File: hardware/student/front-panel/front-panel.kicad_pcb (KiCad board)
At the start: 4 copper layers, 180 x 100 mm, 78 parts, among them J1 Panel link 2x20 female, J10 SMA, J11 SMA, J12 SMA, J13 SMA, J14 SMA, J15 SMA, J16 SMA, J17 SMA, J18 SMA, J19 SMA, J2 Panel link 2x20 female, J20 SMA, J21 SMA, J22 SMA, J23 SMA, J24 SMA, J25 SMA, J26 SMA, J3 Panel link 2x20 female, J30 OLED 0.96in module on 1x4 soc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, J31 KF128-2.54-10P, J32 KF128-5.0-2P, J33 Qwiic (vertical), J40 Module header 2x6 (shrouded), J411 KF301-5.0-2P, J412 KF301-5.0-2P, Q411 MMBT5551, Q412 MMBT5551, Q421 MMBT5551, Q422 MMBT5551, U401 6N137S-TA1-L, U402 6N137S-TA1-L, U410 SN74AHCT541PWR

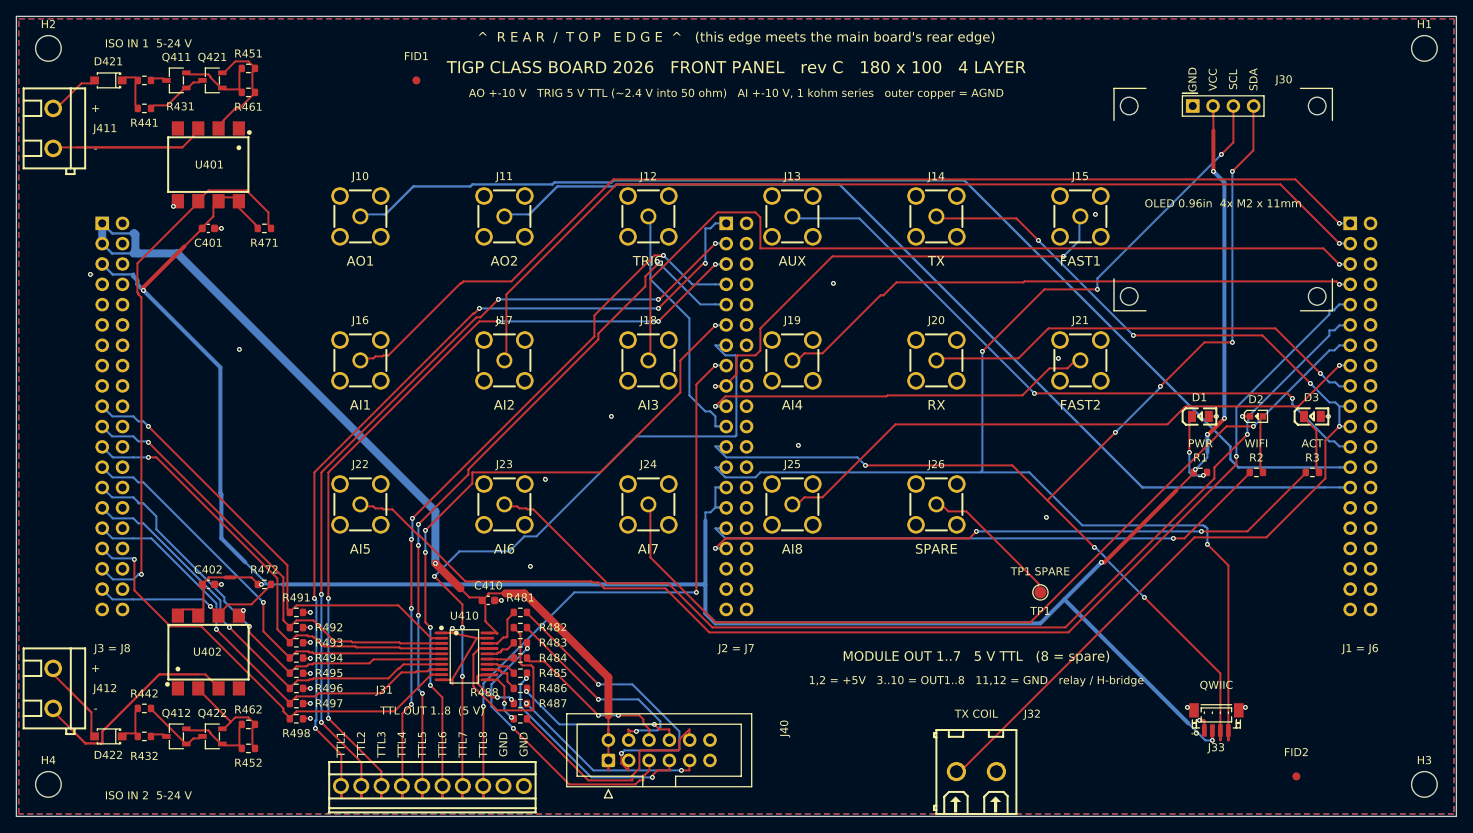
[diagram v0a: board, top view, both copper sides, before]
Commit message: v0.7d: relays and mains removed, MODULE OUT 1-7 (5 V TTL) on a shrouded 2x6 header on the front panel, isolated inputs moved to the panel, section C = the front-panel board (4-layer, 18 mm SMA grid, OLED clear of headers, unrouted student copy), main board re-placed; workbook, tutor guide, firmware docs, hardware docs updated (Decision #58)
Co-Authored-By: Claude Fable 5.1 <noreply@anthropic.com>
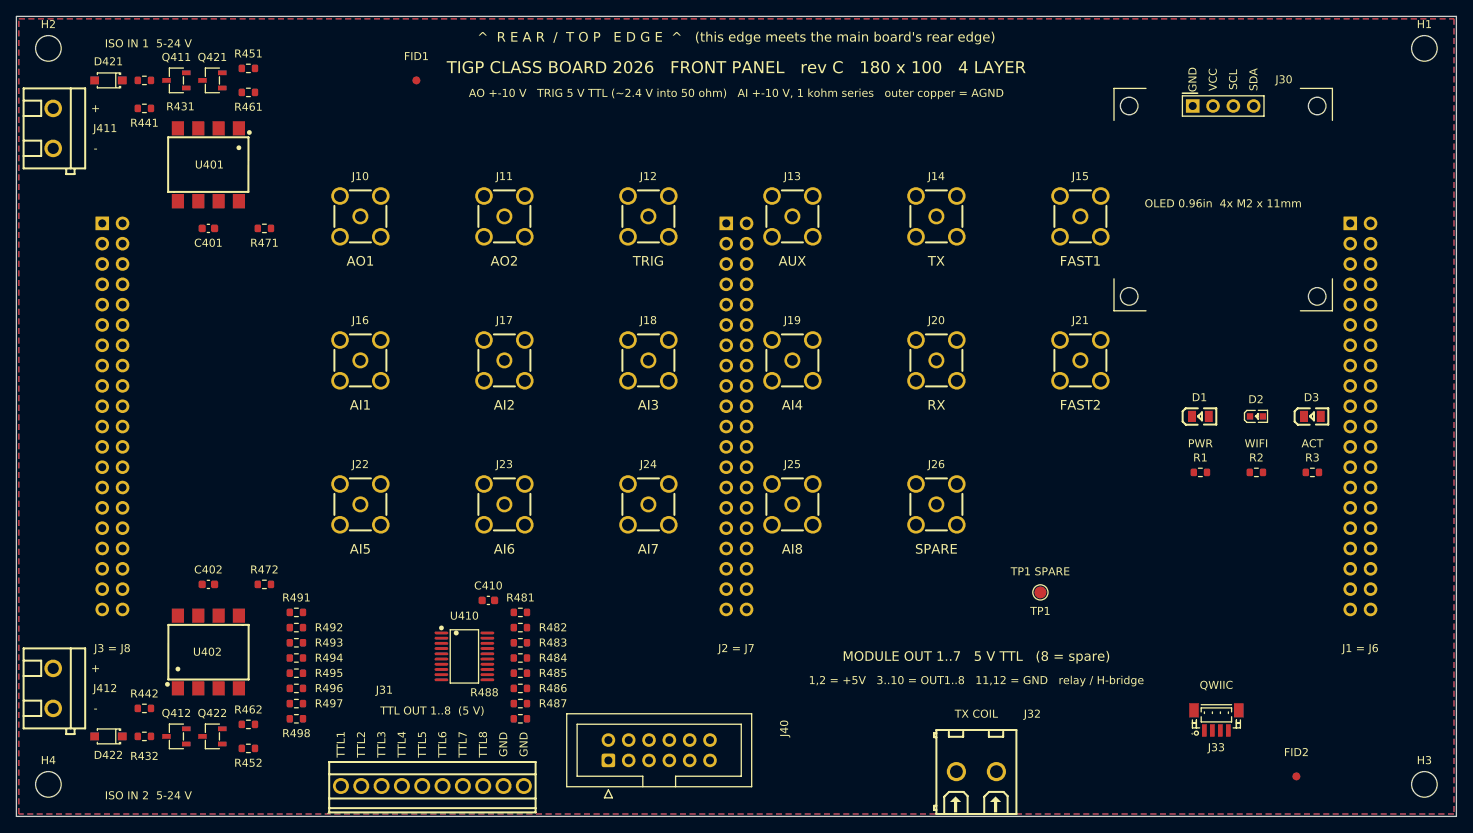
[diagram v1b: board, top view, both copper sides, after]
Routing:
- net +3V3: track 297.3 -> 0.00 mm, vias 8 -> 0
- net I2C_SCL: track 158.2 -> 0.00 mm, vias 4 -> 0
- net AI5: track 150.9 -> 0.00 mm, vias 1 -> 0
- net I2C_SDA: track 148.0 -> 0.00 mm, vias 7 -> 0
- net AO1: track 140.4 -> 0.00 mm
- net AI1: track 134.4 -> 0.00 mm, vias 1 -> 0
- net TX: track 131.8 -> 0.00 mm, vias 4 -> 0
- net AI6: track 129.2 -> 0.00 mm, vias 1 -> 0
- net AO2: track 122.1 -> 0.00 mm
- net AI2: track 121.6 -> 0.00 mm, vias 1 -> 0
- net +5V_RAW: track 118.9 -> 0.00 mm, vias 1 -> 0
- net AI7: track 110.9 -> 0.00 mm, vias 1 -> 0
- net TTL1: track 110.6 -> 0.00 mm, vias 5 -> 0
- net TTL2: track 106.6 -> 0.00 mm, vias 5 -> 0
- net TTL3: track 105.3 -> 0.00 mm, vias 5 -> 0
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
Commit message: front panel: OLED footprint per the real module (27 x 29 mm, holes 24 x 26 mm, header 1 mm below the top edge), panel + student copy regenerated, DRC 0/0 with zones filled
Co-Authored-By: Claude Fable 5.1 <noreply@anthropic.com>
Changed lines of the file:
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@@
 		(layer "F.Cu")
 		(at 150.85 11.2 0)
-		(descr "0.96 in 128x64 I2C OLED module (4-pin GND VCC SCL SDA, 27.3 x 27.8 mm PCB) plugged into a vertical 1x4 2.54 mm female header 8.5 mm tall (XFCN PZ254-1-04-Z-8.5, LCSC C2894927); the module lies flat 11 mm above the board and is held by four M2 screws through its corner holes (23.5 x 23.8 mm, verify on the real module) into M2 stand-offs. Anchor = centre of the pad row (the socket, the part JLC places). Courtyard = socket + the four holes only: the module body hangs 11 mm above the board and may overhang other parts.")
+		(descr "0.96 in 128x64 I2C OLED module (4-pin GND VCC SCL SDA, 27 x 29 mm PCB (GM009605v4)) plugged into a vertical 1x4 2.54 mm female header 8.5 mm tall (XFCN PZ254-1-04-Z-8.5, LCSC C2894927); the module lies flat 11 mm above the board and is held by four M2 screws through its corner holes (2.4 mm holes at 24 x 26 mm, header body 1 mm below the top edge so the pin row is 2.27 mm below it and the top holes 0.77 mm above the pin row - the instructor's numbers, 2026-09-17, to be confirmed on the delivered modules; the housing front cover clamps the module anyway, Decision #61) into M2 stand-offs. Anchor = centre of the pad row (the socket, the part JLC places). Courtyard = socket + the four holes only: the module body hangs 11 mm above the board and may overhang other parts.")
 		(tags "OLED SSD1306 0.96 module socket M2")
 		(property "Reference" "J30" (at 7.6 -3.3 0) (layer "F.SilkS") (effects (font (size 1 1) (thickness 0.15))))
@@
 		(fp_line (start 5.1 -1.27) (end 5.1 1.27) (stroke (width 0.12) (type solid)) (layer "F.SilkS"))
 		(fp_line (start -5.1 -1.6) (end -3.2 -1.6) (stroke (width 0.2) (type solid)) (layer "F.SilkS"))
-		(fp_line (start -13.65 -2.2) (end -9.65 -2.2) (stroke (width 0.15) (type solid)) (layer "F.SilkS"))
-		(fp_line (start -13.65 -2.2) (end -13.65 1.8) (stroke (width 0.15) (type solid)) (layer "F.SilkS"))
-		(fp_line (start 13.65 -2.2) (end 9.65 -2.2) (stroke (width 0.15) (type solid)) (layer "F.SilkS"))
-		(fp_line (start 13.65 -2.2) (end 13.65 1.8) (stroke (width 0.15) (type solid)) (layer "F.SilkS"))
-		(fp_line (start -13.65 25.6) (end -9.65 25.6) (stroke (width 0.15) (type solid)) (layer "F.SilkS"))
-		(fp_line (start -13.65 25.6) (end -13.65 21.6) (stroke (width 0.15) (type solid)) (layer "F.SilkS"))
-		(fp_line (start 13.65 25.6) (end 9.65 25.6) (stroke (width 0.15) (type solid)) (layer "F.SilkS"))
-		(fp_line (start 13.65 25.6) (end 13.65 21.6) (stroke (width 0.15) (type solid)) (layer "F.SilkS"))
-		(fp_text user "OLED 0.96in  4x M2 x 11mm" (at 0 12.2 0.0) (layer "F.SilkS") (effects (font (size 1 1) (thickness 0.15))))
+		(fp_line (start -13.5 -2.27) (end -9.5 -2.27) (stroke (width 0.15) (type solid)) (layer "F.SilkS"))
+		(fp_line (start -13.5 -2.27) (end -13.5 1.73) (stroke (width 0.15) (type solid)) (layer "F.SilkS"))
+		(fp_line (start 13.5 -2.27) (end 9.5 -2.27) (stroke (width 0.15) (type solid)) (layer "F.SilkS"))
+		(fp_line (start 13.5 -2.27) (end 13.5 1.73) (stroke (width 0.15) (type solid)) (layer "F.SilkS"))
+		(fp_line (start -13.5 26.73) (end -9.5 26.73) (stroke (width 0.15) (type solid)) (layer "F.SilkS"))
+		(fp_line (start -13.5 26.73) (end -13.5 22.73) (stroke (width 0.15) (type solid)) (layer "F.SilkS"))
+		(fp_line (start 13.5 26.73) (end 9.5 26.73) (stroke (width 0.15) (type solid)) (layer "F.SilkS"))
+		(fp_line (start 13.5 26.73) (end 13.5 22.73) (stroke (width 0.15) (type solid)) (layer "F.SilkS"))
+		(fp_text user "OLED 0.96in  4x M2 x 11mm" (at 0 13.0 0.0) (layer "F.SilkS") (effects (font (size 1 1) (thickness 0.15))))
 		(fp_text user "GND" (at -3.81 -3.3 90.0) (layer "F.SilkS") (effects (font (size 1 1) (thickness 0.15))))
 		(fp_text user "VCC" (at -1.27 -3.3 90.0) (layer "F.SilkS") (effects (font (size 1 1) (thickness 0.15))))
 		(fp_text user "SCL" (at 1.27 -3.3 90.0) (layer "F.SilkS") (effects (font (size 1 1) (thickness 0.15))))
 		(fp_text user "SDA" (at 3.81 -3.3 90.0) (layer "F.SilkS") (effects (font (size 1 1) (thickness 0.15))))
-		(fp_rect (start -13.65 -2.2) (end 13.65 25.6) (stroke (width 0.1) (type solid)) (fill no) (layer "F.Fab"))
-		(fp_rect (start -13.35 3.3) (end 13.35 22.6) (stroke (width 0.1) (type solid)) (fill no) (layer "F.Fab"))
+		(fp_rect (start -13.5 -2.27) (end 13.5 26.73) (stroke (width 0.1) (type solid)) (fill no) (layer "F.Fab"))
+		(fp_rect (start -13.35 3.23) (end 13.35 22.53) (stroke (width 0.1) (type solid)) (fill no) (layer "F.Fab"))
 		(fp_rect (start -5.1 -1.27) (end 5.1 1.27) (stroke (width 0.1) (type solid)) (fill no) (layer "F.Fab"))
 		(fp_line (start -5.1 -1.27) (end -4.4 -0.5) (stroke (width 0.1) (type solid)) (layer "F.Fab"))
 		(fp_rect (start -5.35 -1.55) (end 5.35 1.55) (stroke (width 0.05) (type solid)) (fill no) (layer "F.CrtYd"))
-		(fp_rect (start -13.15 -1.4) (end -10.35 1.4) (stroke (width 0.05) (type solid)) (fill no) (layer "F.CrtYd"))
-		(fp_rect (start 10.35 -1.4) (end 13.15 1.4) (stroke (width 0.05) (type solid)) (fill no) (layer "F.CrtYd"))
-		(fp_rect (start -13.15 22.4) (end -10.35 25.2) (stroke (width 0.05) (type solid)) (fill no) (layer "F.CrtYd"))
-		(fp_rect (start 10.35 22.4) (end 13.15 25.2) (stroke (width 0.05) (type solid)) (fill no) (layer "F.CrtYd"))
+		(fp_rect (start -13.4 -2.17) (end -10.6 0.63) (stroke (width 0.05) (type solid)) (fill no) (layer "F.CrtYd"))
+		(fp_rect (start 10.6 -2.17) (end 13.4 0.63) (stroke (width 0.05) (type solid)) (fill no) (layer "F.CrtYd"))
+		(fp_rect (start -13.4 23.83) (end -10.6 26.63) (stroke (width 0.05) (type solid)) (fill no) (layer "F.CrtYd"))
+		(fp_rect (start 10.6 23.83) (end 13.4 26.63) (stroke (width 0.05) (type solid)) (fill no) (layer "F.CrtYd"))
 		(pad 1 thru_hole rect (at -3.81 0 0.0) (size 1.7 1.7) (drill 1) (layers "*.Cu" "*.Mask") (remove_unused_layers no) (net 2 "GND"))
 		(pad 2 thru_hole circle (at -1.27 0 0.0) (size 1.7 1.7) (drill 1) (layers "*.Cu" "*.Mask") (remove_unused_layers no) (net 1 "+3V3"))
 		(pad 3 thru_hole circle (at 1.27 0 0.0) (size 1.7 1.7) (drill 1) (layers "*.Cu" "*.Mask") (remove_unused_layers no) (net 37 "I2C_SCL"))
 		(pad 4 thru_hole circle (at 3.81 0 0.0) (size 1.7 1.7) (drill 1) (layers "*.Cu" "*.Mask") (remove_unused_layers no) (net 36 "I2C_SDA"))
-		(pad "" np_thru_hole circle (at -11.75 0 0.0) (size 2.2 2.2) (drill 2.2) (layers "*.Cu" "*.Mask"))
-		(pad "" np_thru_hole circle (at 11.75 0 0.0) (size 2.2 2.2) (drill 2.2) (layers "*.Cu" "*.Mask"))
-		(pad "" np_thru_hole circle (at -11.75 23.8 0.0) (size 2.2 2.2) (drill 2.2) (layers "*.Cu" "*.Mask"))
-		(pad "" np_thru_hole circle (at 11.75 23.8 0.0) (size 2.2 2.2) (drill 2.2) (layers "*.Cu" "*.Mask"))
+		(pad "" np_thru_hole circle (at -12 -0.77 0.0) (size 2.4 2.4) (drill 2.4) (layers "*.Cu" "*.Mask"))
+		(pad "" np_thru_hole circle (at 12 -0.77 0.0) (size 2.4 2.4) (drill 2.4) (layers "*.Cu" "*.Mask"))
+		(pad "" np_thru_hole circle (at -12 25.23 0.0) (size 2.4 2.4) (drill 2.4) (layers "*.Cu" "*.Mask"))
+		(pad "" np_thru_hole circle (at 12 25.23 0.0) (size 2.4 2.4) (drill 2.4) (layers "*.Cu" "*.Mask"))
 		(model "${KICAD10_3DMODEL_DIR}/Connector_PinSocket_2.54mm.3dshapes/PinSocket_1x04_P2.54mm_Vertical.step" (offset (xyz -3.81 0 0)) (scale (xyz 1 1 1)) (rotate (xyz 0 0 90)))
 		(model "${KIPRJMOD}/../../lib/class_board.3dshapes/OLED-0.96in-4P-module.wrl" (offset (xyz 0 0 0)) (scale (xyz 1 1 1)) (rotate (xyz 0 0 0)))

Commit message: front panel: male link headers J1/J2/J3 (Decision #62), J1 escapes outward; routed, DRC 0/0 with zones filled; student copy regenerated
Co-Authored-By: Claude Fable 5.1 <noreply@anthropic.com>
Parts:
- J1, J2, J3: value Panel link 2x20 female -> Panel link 2x20 male; footprint Connector_PinSocket_2.54mm:PinSocket_2x20_P2.54mm_Vertical -> Connector_PinHeader_2.54mm:PinHeader_2x20_P2.54mm_Vertical
- moved J1 2.54 mm to (169.3, 25.9)
- moved J3 2.54 mm to (13.3, 25.9)
- moved J2 2.54 mm to (91.3, 25.9)
